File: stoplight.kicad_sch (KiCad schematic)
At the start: 46 parts, among them J1 Conn_01x04_Socket, J2 Conn_01x04_Socket, Q1 DOZ30P03, U1 HUSB238_002DD, U3 TMC2209-LA-T, U4 DS18B20U, U5 TPS54202DDCR

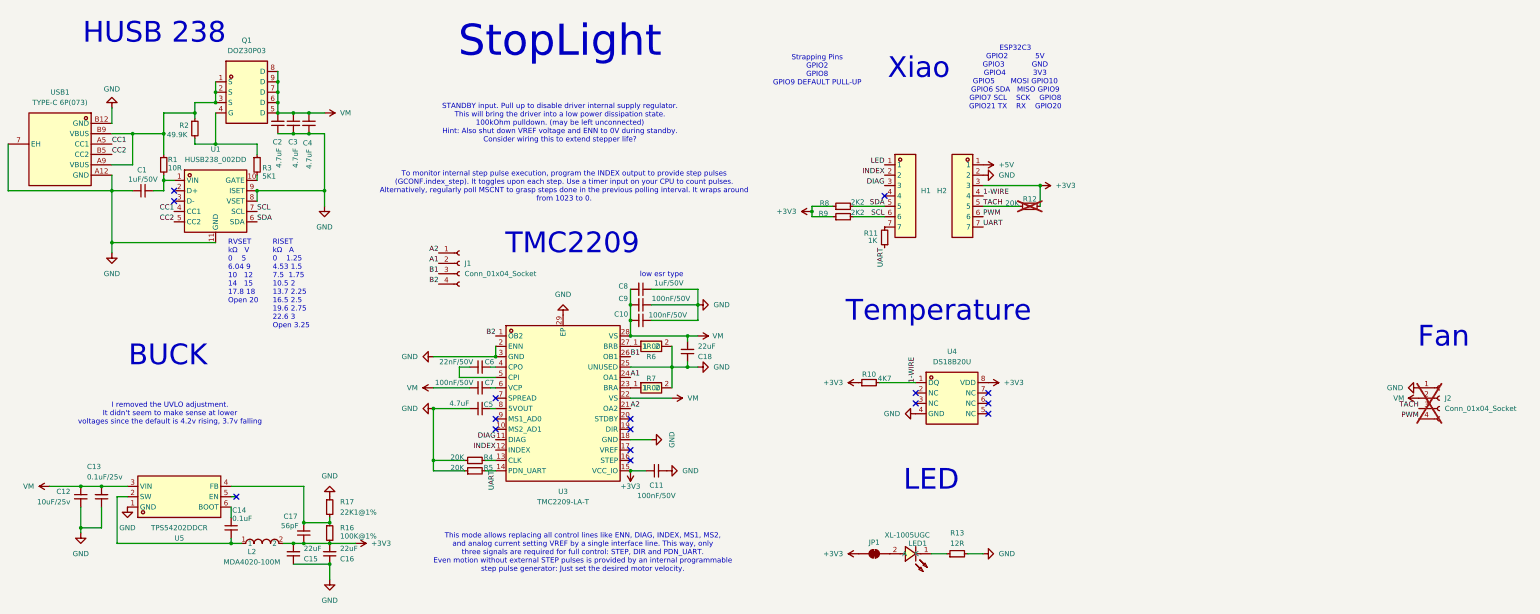
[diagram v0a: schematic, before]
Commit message: add power pours and additional vias
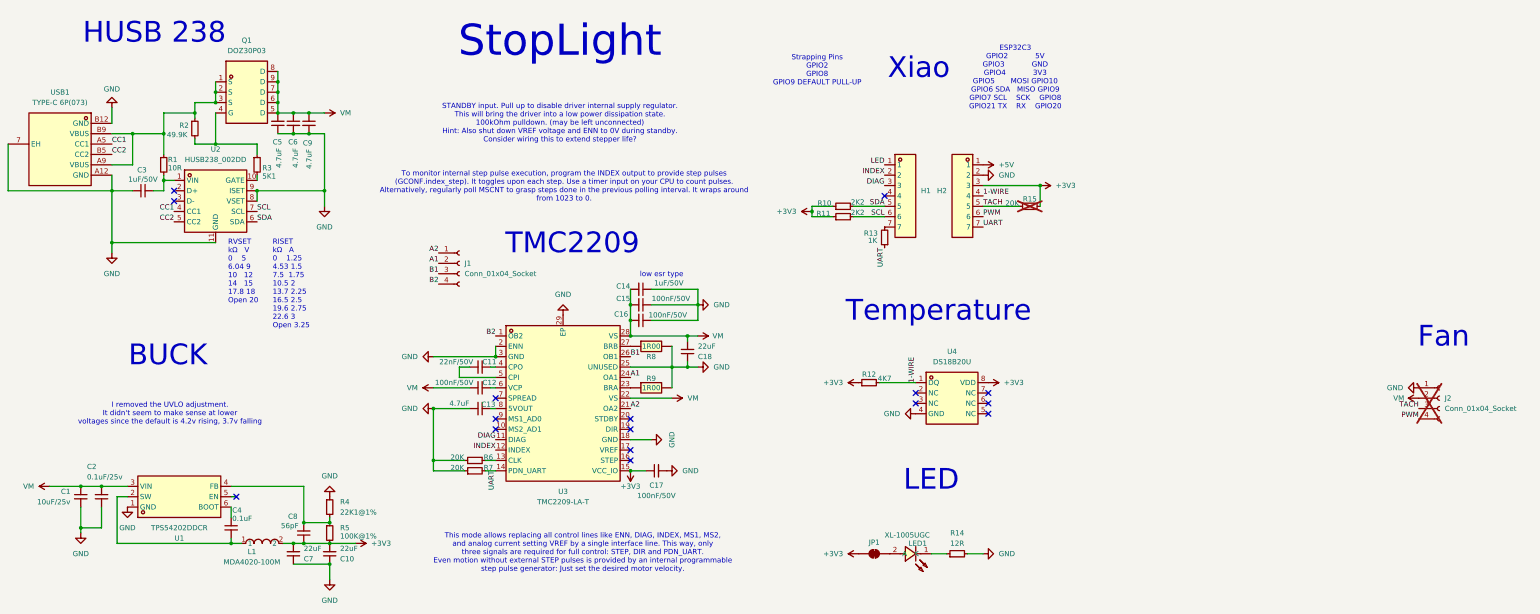
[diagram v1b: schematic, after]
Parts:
- C1: renamed from C12; LCSC (none) -> C2918502
- C11: renamed from C6; LCSC (none) -> C77023
- C12: renamed from C7; LCSC (none) -> C77020
- C13: renamed from C5; LCSC (none) -> C913474
- C14: renamed from C8; LCSC (none) -> C90540
- C15: renamed from C9; LCSC (none) -> C77020
- C16: renamed from C10; LCSC (none) -> C77020
- C17: renamed from C11; LCSC (none) -> C77020
- C2: renamed from C13; LCSC (none) -> C3011652
- C4: renamed from C14; LCSC (none) -> C77020
- C5: renamed from C2; LCSC (none) -> C2991173
- C6: renamed from C3; LCSC (none) -> C2991173
- C8: renamed from C17; LCSC (none) -> C107007
- C9: renamed from C4; LCSC (none) -> C2991173
- J1: LCSC (none) -> C23398778
- R1: LCSC (none) -> C109318
- R10: renamed from R8; LCSC (none) -> C114762
- R11: renamed from R9; LCSC (none) -> C114762
- R12: renamed from R10; LCSC (none) -> C105871
- R13: renamed from R11; LCSC (none) -> C22548
- R2: LCSC (none) -> C2930109
- R3: LCSC (none) -> C23186
- R4: renamed from R17; LCSC (none) -> C163478
- R5: renamed from R16; LCSC (none) -> C60491
- R6: renamed from R4; LCSC (none) -> C93942
- R7: renamed from R5; LCSC (none) -> C93942
- renumbered C16 to C10, C1 to C3, C15 to C7, L2 to L1, R13 to R14, R12 to R15, R6 to R8, R7 to R9, U5 to U1, U1 to U2
